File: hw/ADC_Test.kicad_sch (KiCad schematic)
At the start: 119 parts, among them J1 SMA SENSOR IN, J3 PMOD (ZedBoard), J4 SMA MON, J6 SMA HEAD OUT, J7 3V3 IN, U1 OPA2365, U2 OPA2365, U3 THS4531, U4 ADS7057, U6 TLV7022, U8 OPA365, U9 TLV7022

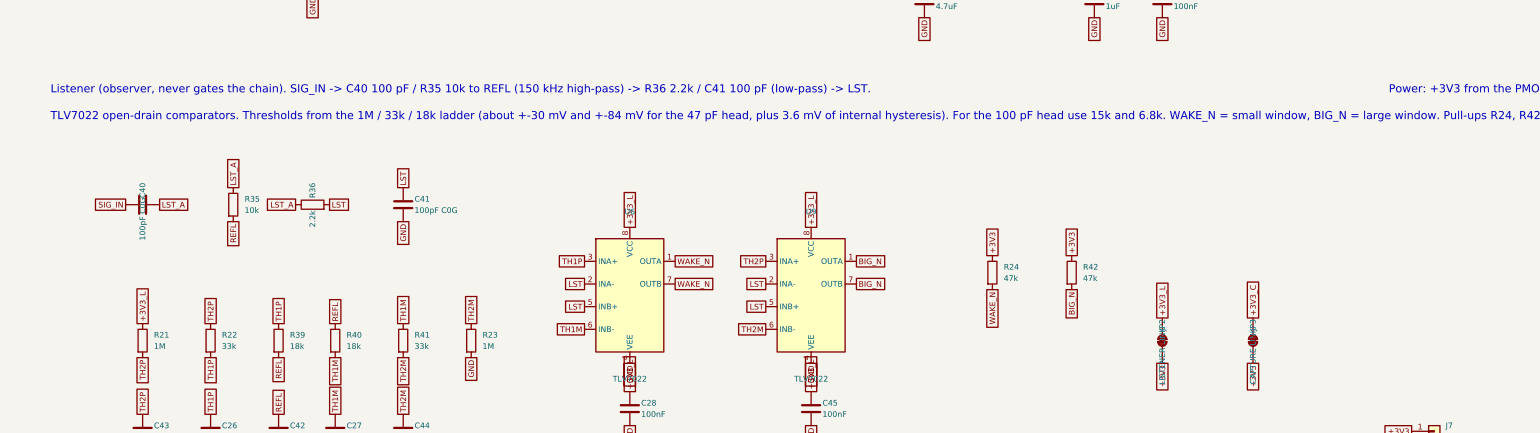
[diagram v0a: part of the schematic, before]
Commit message: Listener filter fix found by the netlist simulation: R36 10k, C41 22 pF, R39/R40 15k; sim/netlist_verify.py; manual and README updated
Co-Authored-By: Claude Sonnet 5.5 <noreply@anthropic.com>
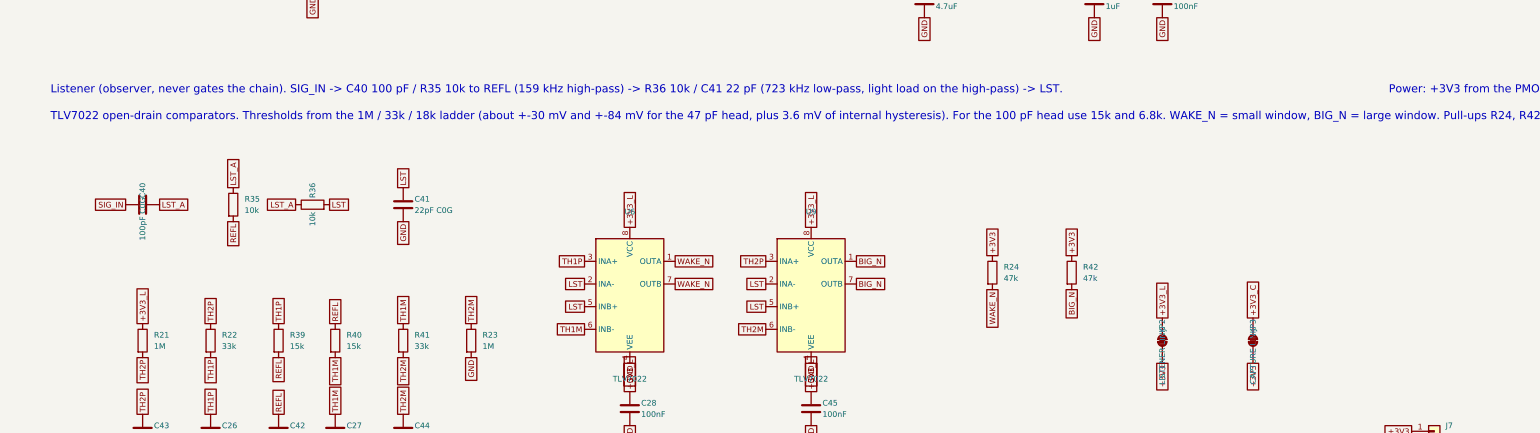
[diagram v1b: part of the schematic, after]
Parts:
- C41: value 100pF C0G -> 22pF C0G; LCSC C14858 -> C1653
- R36: value 2.2k -> 10k; LCSC C4190 -> C25804
- R39, R40: value 18k -> 15k; LCSC C25810 -> C22809
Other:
- note added: "Listener (observer, never gates the chain). SIG_IN -> C40 100 pF / R35 10k to REFL (159 kHz high-pass) -> R36 10k / C41 22 pF (723 kHz low-pass, light load on the high-pass) -> LST."
- note removed: "Listener (observer, never gates the chain). SIG_IN -> C40 100 pF / R35 10k to REFL (150 kHz high-pass) -> R36 2.2k / C41 100 pF (low-pass) -> LST."

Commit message: Power: 5-pin SMU header J7 replaces JP2/JP4/JP5/JP6 and the 2-pin header; top silkscreen with TP and IC numbers; slides and README updated
Co-Authored-By: Claude Sonnet 5.5 <noreply@anthropic.com>
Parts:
- removed J7: 3V3 IN, Connector_PinHeader_2.54mm:PinHeader_1x02_P2.54mm_Vertical, symbol Connector_Generic:Conn_01x02
- removed JP2: LISTENER LINK, Jumper:SolderJumper-2_P1.3mm_Bridged_Pad1.0x1.5mm, symbol Jumper:SolderJumper_2_Bridged
- removed JP4: AVDD LINK, Jumper:SolderJumper-2_P1.3mm_Bridged_Pad1.0x1.5mm, symbol Jumper:SolderJumper_2_Bridged
- removed JP5: DVDD LINK, Jumper:SolderJumper-2_P1.3mm_Bridged_Pad1.0x1.5mm, symbol Jumper:SolderJumper_2_Bridged
- removed JP6: PMOD 3V3, Jumper:SolderJumper-2_P1.3mm_Bridged_Pad1.0x1.5mm, symbol Jumper:SolderJumper_2_Bridged
- added J7: POWER / SMU, Connector_PinHeader_2.54mm:PinHeader_1x05_P2.54mm_Vertical, symbol Connector_Generic:Conn_01x05
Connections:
- net +3V3_L is gone; now on net +3V3: C28.1, C45.1, R21.1, U6.8 (VCC), U9.8 (VCC)
- net AVDD_IN is gone; now on net +3V3_C: R34.1
- net DVDD is gone; now on net +3V3: C19.1, C20.1, U4.4 (DVDD)
- net +3V3: now also J7.2 (Pin_2), J7.3 (Pin_3)
- net +3V3_PMOD: now also J7.1 (Pin_1)
- net GND: now also J7.4 (Pin_4), J7.5 (Pin_5)
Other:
- note added: "AVDD = +3V3_C through R34 10R and C21 10 uF. C18 4.7 uF + C22 100 nF sit at the ADS7057 AVDD pin. DVDD = +3V3."
- note added: "Power header J7: 1 Onboard + (PMOD 3.3 V), 2 Force +, 3 Sense +, 4 Sense -, 5 Force -. Jumper 1-2 powers the board from the PMOD. For a source-measure unit remove the jumper and connect Force to 2 and 5, Sense to 3 and 4. JP3 (closed) joins the capture rail +3V3_C to +3V3: open it to switch or measure the chain separately. JP1 = head power."
- note removed: "AVDD = +3V3_C through JP4 (current link), R34 10R and C21 10 uF. C18 4.7 uF + C22 100 nF sit at the ADS7057 AVDD pin. DVDD = +3V3 through JP5."
- note removed: "Power: +3V3 from the PMOD pins 6 and 12 through JP6 (bridged), or from the 2-pin header J7. Cut JP6 when J7 feeds the board. Current links: JP1 head, JP2 listener, JP3 capture, JP4 AVDD, JP5 DVDD."

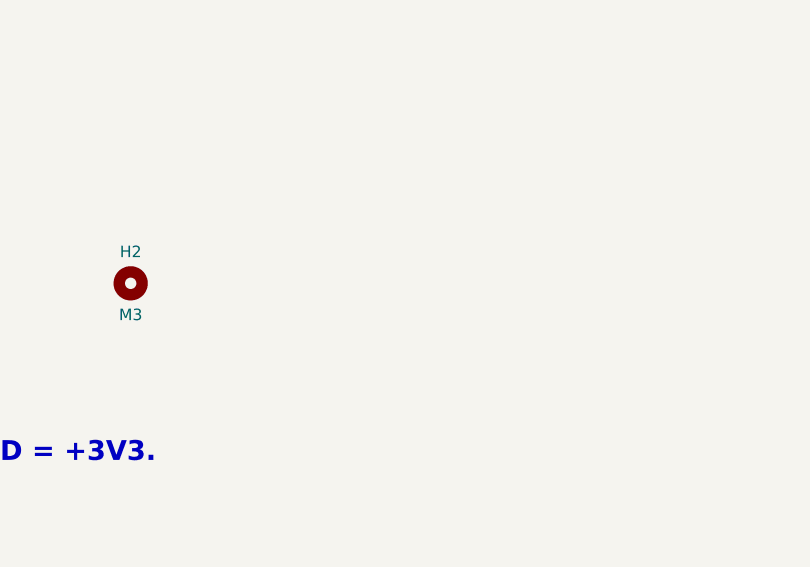
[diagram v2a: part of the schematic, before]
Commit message: Head: two M2 mounting holes (board 10 x 27 mm); JLC CPL: J7 rotation 0 and centre offset, J3 centre offset
Co-Authored-By: Claude Sonnet 5.5 <noreply@anthropic.com>
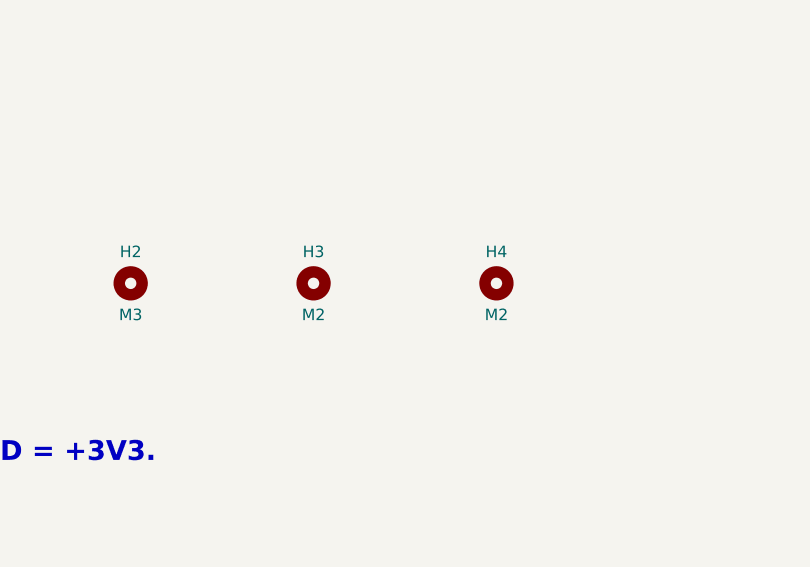
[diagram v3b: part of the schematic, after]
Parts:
- added H3, H4: M2, MountingHole:MountingHole_2.2mm_M2, symbol Mechanical:MountingHole
